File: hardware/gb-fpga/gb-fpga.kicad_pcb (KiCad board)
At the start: 4 copper layers, 80.1 x 78.6 mm, 136 parts, among them J1 USB_C_Receptacle_USB2.0, J2 Cartridge-32pin, J3 BAT+, J4 BAT-, J5 Conn_02x25_Counter_Clockwise, Q1 MBT3904DW1, SW1 Switch, U1 xc7s25ftgb196, U2 MX25R3235FZBxx1, U3 FT2232HQ, U4 LTC3555, U5 TLV61046ADB, U6 TXS0108E, U7 TXS0108E, U8 TXS0108E, U9 TXS0108E, X1 SG-8002JA

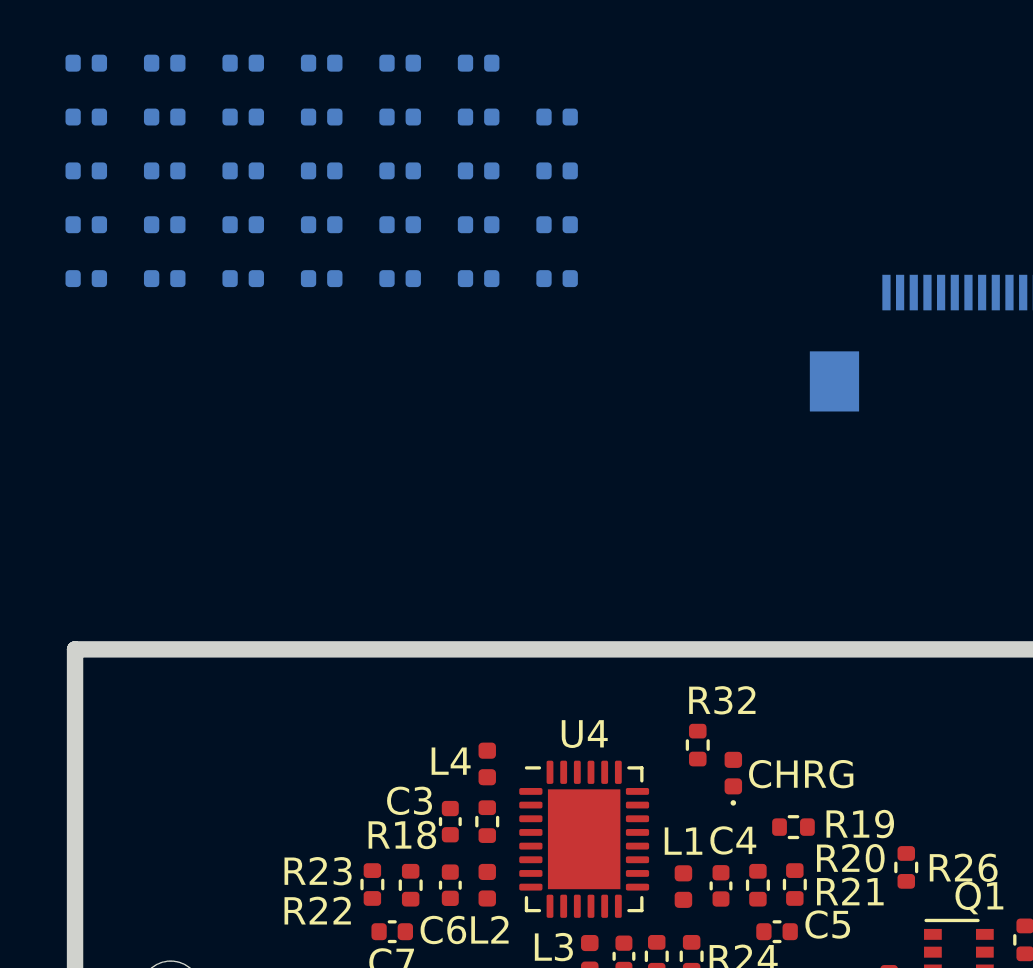
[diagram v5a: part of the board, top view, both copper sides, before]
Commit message: Switch to 0201 footprints for fpga power caps
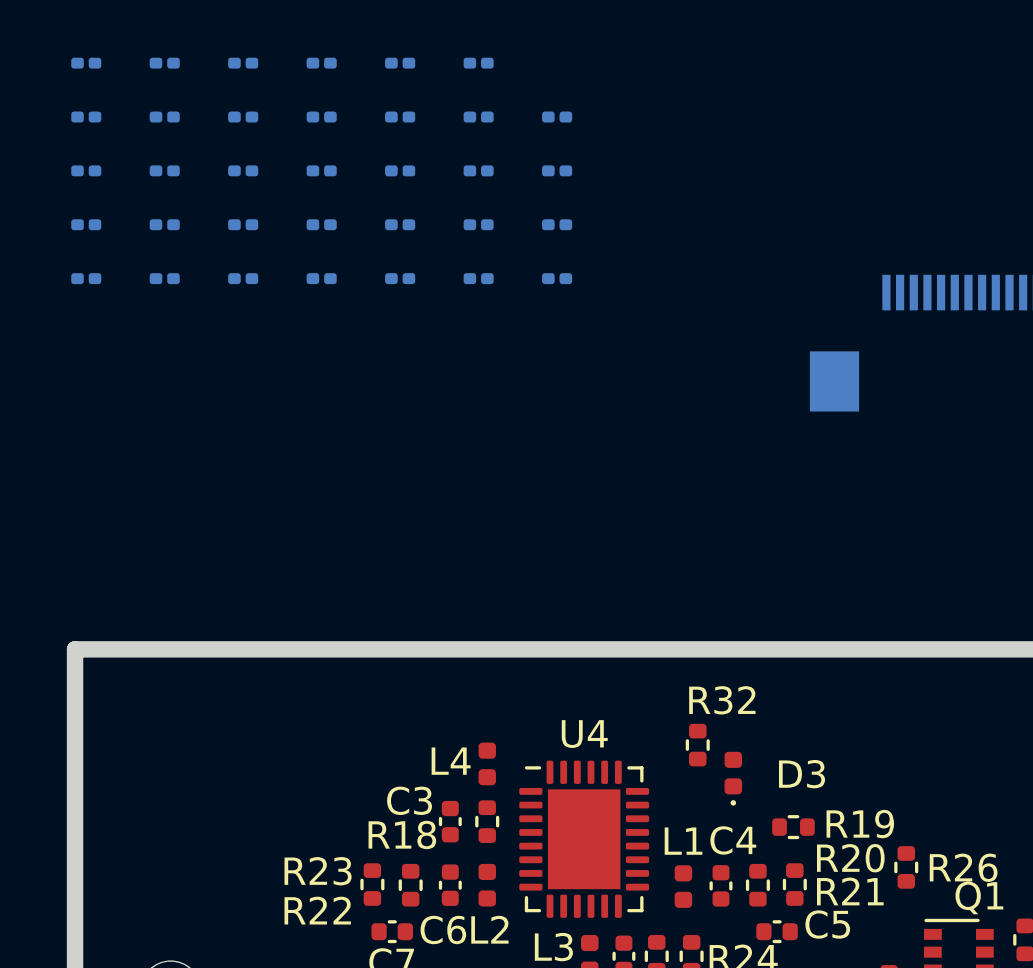
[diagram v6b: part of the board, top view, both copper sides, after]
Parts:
- C14, C15, C16, C17, C18, C19, C20, C21, C22, C23, C24, C25, C26, C27, C28, C29, C30, C31, C32, C33, C34, C35, C36, C37, C38, C39, C40, C41, C42, C43, C44, C45, C46, C47: footprint Capacitor_SMD:C_0402_1005Metric -> Capacitor_SMD:C_0201_0603Metric
- renumbered CHRG to D3
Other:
- net class Default: clearance 0.2 -> 0.15
- rule trace_clearance: 0.2 -> 0.15

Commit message: Place most fpga caps
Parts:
- moved C17 70.1 mm to (52.7, -49.3), turned to 270 degrees
- moved C24 67.2 mm to (48.7, -53.3), turned to 90 degrees
- moved C20 65.1 mm to (47.7, -53.3), turned to 270 degrees
- moved C14 64.5 mm to (48.7, -49.3), turned to 270 degrees
- moved C26 63.9 mm to (49.7, -49.3), turned to 90 degrees
- moved C30 63.9 mm to (40.7, -44.3), turned to 270 degrees
- moved C25 63.3 mm to (43.7, -49.3), turned to 270 degrees
- moved C21 62.5 mm to (44.7, -49.3), turned to 90 degrees
- moved C15 61.6 mm to (42.7, -49.3), turned to 90 degrees
- moved C16 61.0 mm to (45.7, -48.3), turned to 90 degrees
- moved C47 59.7 mm to (43.7, -44.3), turned to 270 degrees
- moved C23 57.7 mm to (47.7, -49.3), turned to 90 degrees
- moved C18 57.4 mm to (43.7, -53.3), turned to 90 degrees
- moved C33 57.2 mm to (47.7, -45.3), turned to 90 degrees
- moved C22 56.1 mm to (44.7, -53.3), turned to 270 degrees
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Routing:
- net GND: track 38.3 -> 38.7 mm, vias 53 -> 54

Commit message: Assign cartridge pins to fpga
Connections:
- U1 pad A12: Net-(U1-PadA12) -> GB_D7
- U1 pad A13: Net-(U1-PadA13) -> GB_D5
- U1 pad B13: Net-(U1-PadB13) -> GB_D3
- U1 pad B14: Net-(U1-PadB14) -> GB_D2
- U1 pad C12: Net-(U1-PadC12) -> GB_D6
- U1 pad C14: Net-(U1-PadC14) -> GB_D1
- U1 pad D12: Net-(U1-PadD12) -> GB_D4
- U1 pad D13: Net-(U1-PadD13) -> GB_D0
- U1 pad D14: Net-(U1-PadD14) -> GB_RST
- U1 pad E13: Net-(U1-PadE13) -> GB_A15
- U1 pad F13: Net-(U1-PadF13) -> GB_A14
- U1 pad F14: Net-(U1-PadF14) -> GB_A13
- U1 pad G14: Net-(U1-PadG14) -> GB_A12
- U1 pad H13: Net-(U1-PadH13) -> GB_A10
- U1 pad H14: Net-(U1-PadH14) -> GB_A11
- U1 pad J13: Net-(U1-PadJ13) -> GB_A8
- U1 pad J14: Net-(U1-PadJ14) -> GB_A9
- U1 pad L13: Net-(U1-PadL13) -> GB_A6
- U1 pad L14: Net-(U1-PadL14) -> GB_A7
- U1 pad M12: Net-(U1-PadM12) -> GB_A1
- U1 pad M13: Net-(U1-PadM13) -> GB_A4
- U1 pad M14: Net-(U1-PadM14) -> GB_A5
- U1 pad N10: Net-(U1-PadN10) -> GB_WR
- U1 pad N11: Net-(U1-PadN11) -> GB_CS
- U1 pad N14: Net-(U1-PadN14) -> GB_A3
- U1 pad P10: Net-(U1-PadP10) -> GB_CLK
- U1 pad P11: Net-(U1-PadP11) -> GB_RD
- U1 pad P12: Net-(U1-PadP12) -> GB_A0
- U1 pad P13: Net-(U1-PadP13) -> GB_A2
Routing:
- net Net-(U1-PadD12): track 4.95 -> 0.00 mm, vias 2 -> 0
- net GB_D4: track 0.00 -> 4.95 mm, vias 0 -> 2
- net Net-(U1-PadM12): track 3.75 -> 0.00 mm, vias 2 -> 0
- net GB_A1: track 0.00 -> 3.75 mm, vias 0 -> 2
- net Net-(U1-PadC12): track 2.98 -> 0.00 mm
- net GB_D6: track 0.00 -> 2.98 mm
- net Net-(U1-PadM13): track 1.98 -> 0.00 mm
- net Net-(U1-PadL13): track 1.98 -> 0.00 mm
- net Net-(U1-PadJ13): track 1.98 -> 0.00 mm
- net Net-(U1-PadH13): track 1.98 -> 0.00 mm
- net Net-(U1-PadF13): track 1.98 -> 0.00 mm
- net Net-(U1-PadE13): track 1.98 -> 0.00 mm
- net Net-(U1-PadD13): track 1.98 -> 0.00 mm
- net Net-(U1-PadB13): track 1.98 -> 0.00 mm
- net GB_D3: track 0.00 -> 1.98 mm
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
